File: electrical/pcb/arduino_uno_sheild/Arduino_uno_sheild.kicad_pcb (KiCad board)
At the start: 2 copper layers, 68.6 x 53.3 mm, 16 parts, among them J1 ED10523-ND, J2 6posheader, J3 6posheader, J4 6posheader, J5 6posheader, J6 ED2580-ND, y1 rover_silkscreen

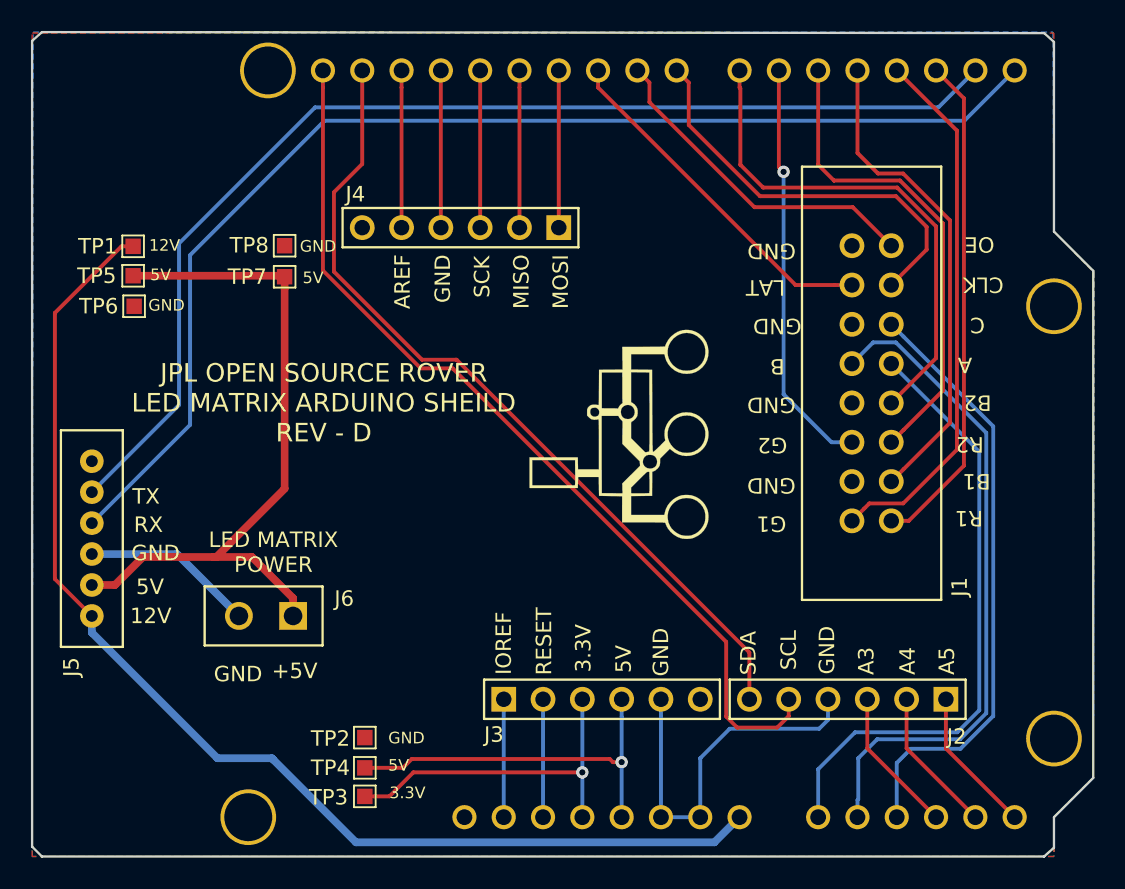
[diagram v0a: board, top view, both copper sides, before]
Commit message: Updates to PCB layout for Arduino shield
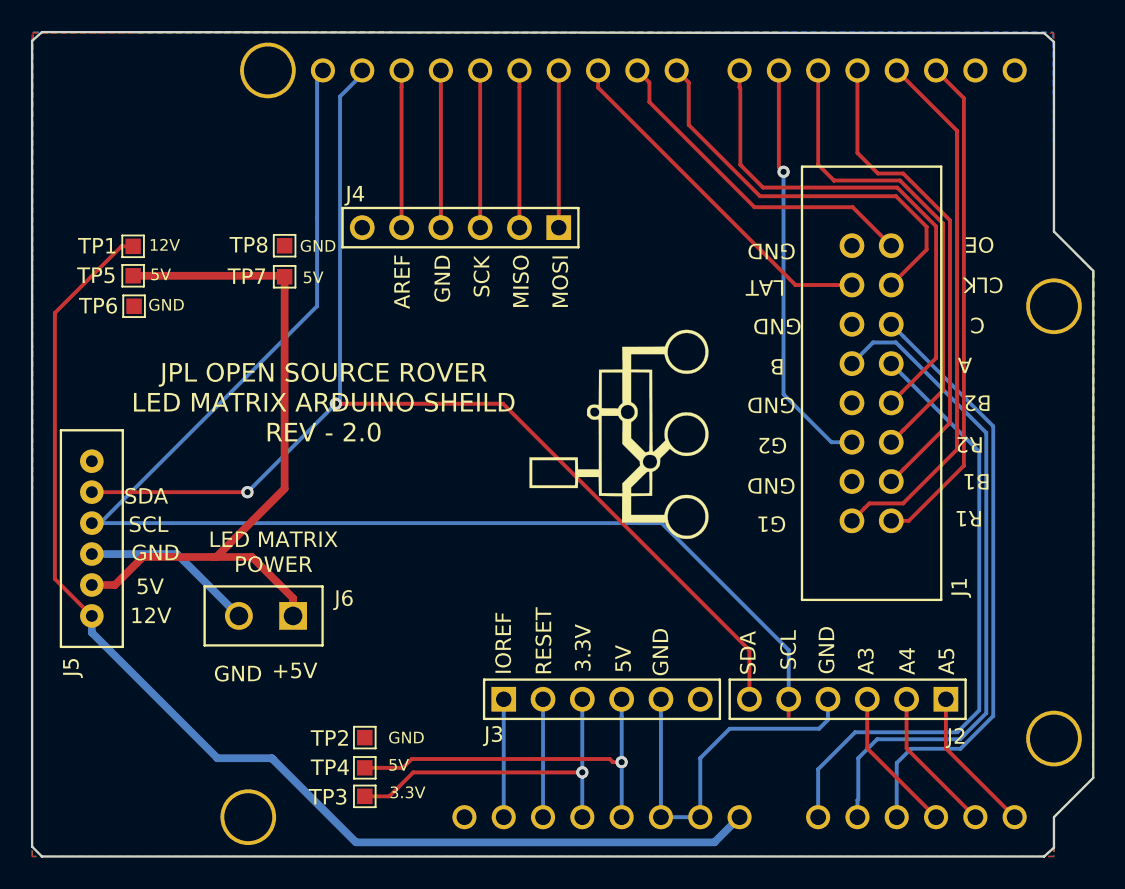
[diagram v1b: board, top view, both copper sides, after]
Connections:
- J5 pad 4: /RX -> /SCL
- J5 pad 5: /TX -> /SDA
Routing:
- net /RX: track 78.2 -> 0.00 mm
- net /TX: track 74.5 -> 0.00 mm
- net /SCL: track 59.5 -> 87.1 mm
- net /SDA: track 53.8 -> 75.4 mm, vias 0 -> 2
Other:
- board text added: "JPL OPEN SOURCE ROVER LED MATRIX ARDUINO SHEILD REV - 2.0"
- board text removed: "JPL OPEN SOURCE ROVER LED MATRIX ARDUINO SHEILD REV - D"
- board text removed: "RX"
- board text removed: "TX"
